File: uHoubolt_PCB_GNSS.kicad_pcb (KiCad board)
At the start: 4 copper layers, 85 x 85 mm, 92 parts, among them J1 Power In, J10 CAN1, J11 CAN2, J12 MMCX-J-P-H-ST-SM1, J2 Debug, J3 Debug, J4 CAN1, J5 CAN2, J6 CAN1, J7 CAN2, J8 CAN1, J9 CAN2, Q1 SISA88DN or similar, U1 SAM-M8Q, U10 LoRa1278F30, U11 LPS25HB, U2 STM32G491MET6-LQFP80, U3 W25Q256JV, U4 MCP1700-3302E, U5 MCP2562FDT-H_SN, U6 MCP2562FDT-H_SN, U7 TS30041, U8 MCP1700-3302E, U9 ICM-20602, X1 TXC-7C

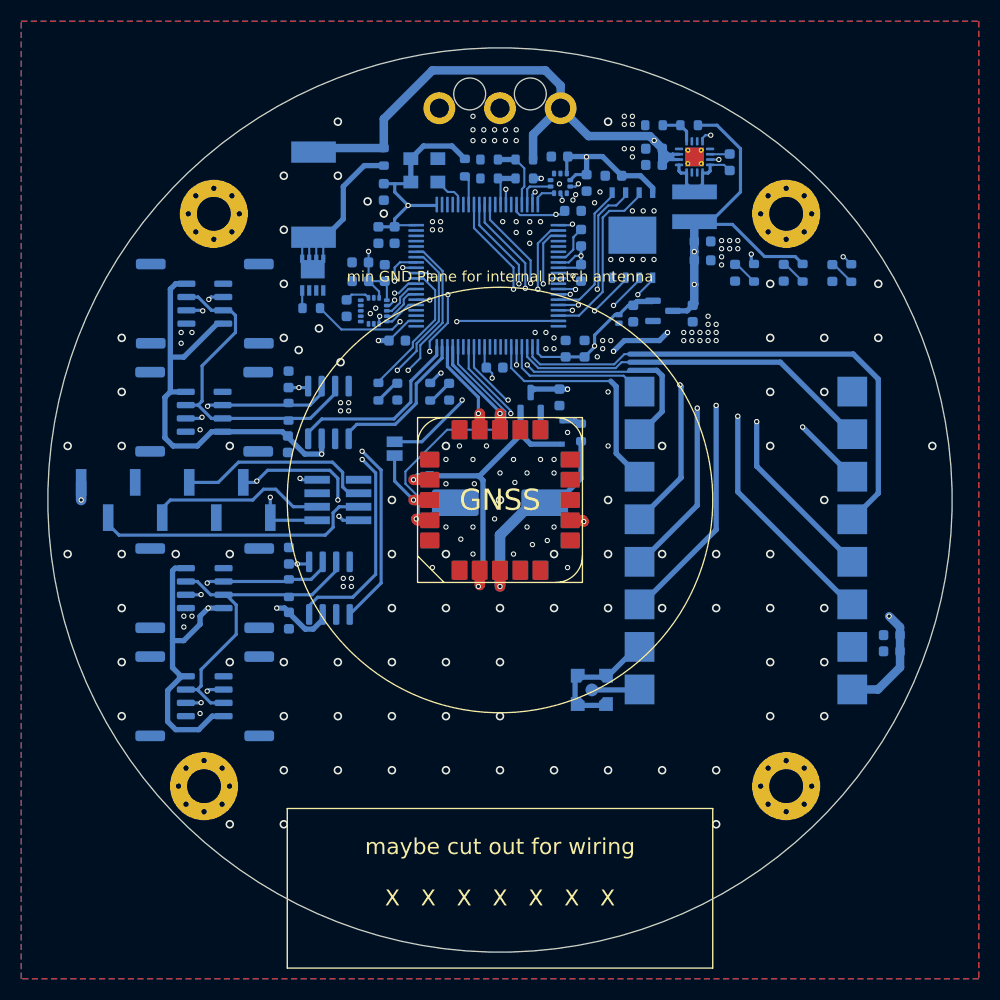
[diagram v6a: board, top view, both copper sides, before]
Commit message: Update CAN transceiver footprints; removed redundant CAN jacks; replaced Power In Conn
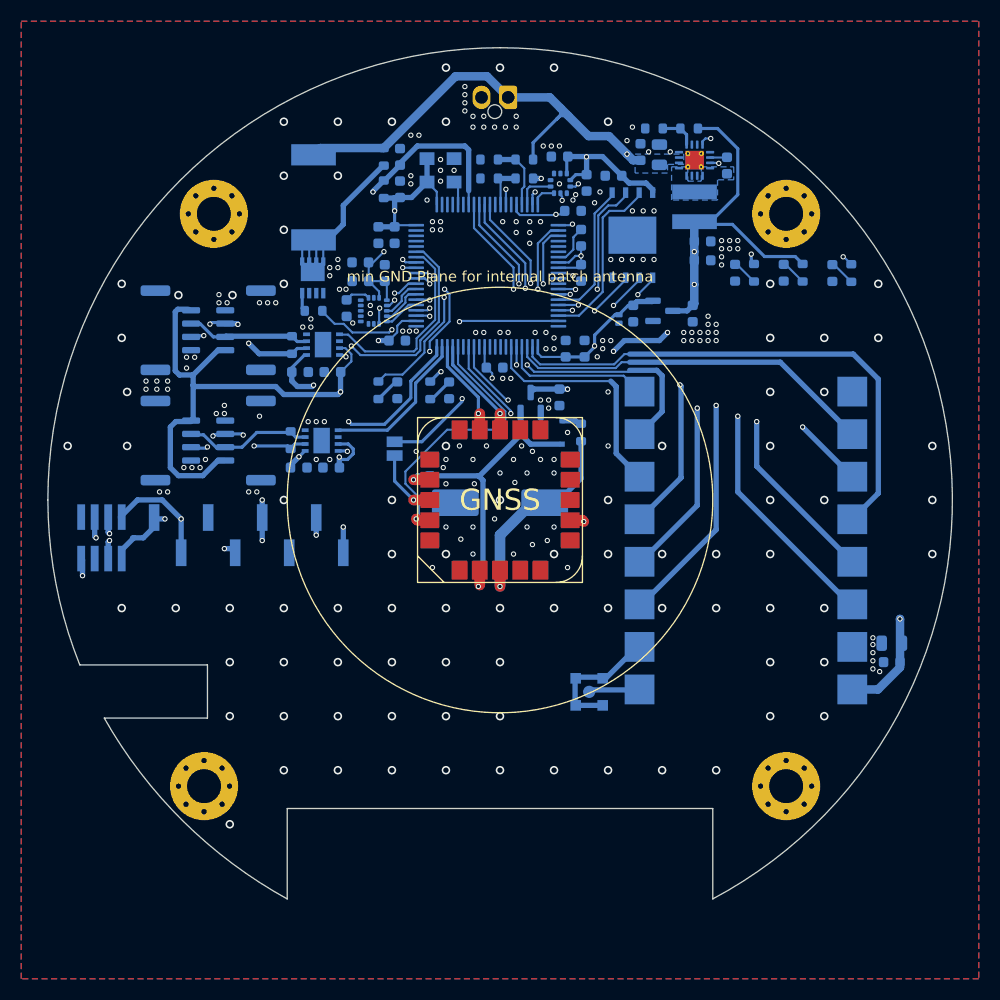
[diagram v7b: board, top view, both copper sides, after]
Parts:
- removed J10, J8: CAN1, Connector_JST:JST_GH_BM04B-GHS-TBT_1x04-1MP_P1.25mm_Vertical
- removed J11, J9: CAN2, Connector_JST:JST_GH_BM04B-GHS-TBT_1x04-1MP_P1.25mm_Vertical
- added C35: 100n, Capacitor_SMD:C_0603_1608Metric, B.Cu at (140.6, 67.7)
- C18, C29: footprint Capacitor_SMD:C_0603_1608Metric -> Capacitor_SMD:C_0805_2012Metric
- J1: footprint TXV_Library_Footprints:Molex_MegaFit_1x03_Vertical -> TXV_Library_Footprints:Molex_Nano-Fit_105309-xx02_1x02_P2.50mm_Vertical
- J12: value MMCX-J-P-H-ST-SM1 -> MMCX-J-P-H-RA-SM1; footprint TXV_Library_Footprints:SAMTEC_MMCX-J-P-H-ST-SM1 -> TXV_Library_Footprints:SAMTEC_MMCX-J-P-H-RA-SM1
- U5, U6: value MCP2562FDT-H_SN -> MCP2562FDT; footprint Package_SO:SOIC-8_3.9x4.9mm_P1.27mm -> Package_DFN_QFN:DFN-8-1EP_3x3mm_P0.65mm_EP1.55x2.4mm
- moved J5 35.1 mm to (119.0, 84.0), turned to -90 degrees
- moved J7 24.2 mm to (126.1, 84.0)
- moved C17 23.7 mm to (134.3, 88.0), turned to 180 degrees
- moved U6 22.9 mm to (133.4, 85.4), turned to 180 degrees
- moved R11 22.9 mm to (130.4, 85.4), turned to -90 degrees
- moved J3 22.5 mm to (112.5, 103.6), turned to -90 degrees
- moved C14 17.3 mm to (131.2, 88.0), turned to 180 degrees
- moved J4 12.9 mm to (126.1, 94.4)
- moved C13 8.35 mm to (131.1, 97.0), turned to 180 degrees
- moved R1 7.89 mm to (139.1, 70.8), turned to 90 degrees
- moved J2 7.61 mm to (126.4, 103.3), turned to 90 degrees
- moved G*** 5.85 mm to (136.5, 115.0)
- moved C16 4.62 mm to (134.1, 97.0), turned to 180 degrees
- moved J6 2.75 mm to (119.0, 94.4)
- moved U5 2.72 mm to (133.2, 94.4), turned to 180 degrees
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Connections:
- R1 pad 2: Net-(R1-Pad2) -> /NRST
- U2 pad 63: unconnected-(U2-Pad63) -> /SWDIO
- U2 pad 64: unconnected-(U2-Pad64) -> /SWCLK
- U2 pad 7: Net-(R1-Pad2) -> /NRST
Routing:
- net /NRST: track 18.7 -> 75.2 mm, vias 0 -> 3
- net +5V: track 258.6 -> 208.0 mm, vias 10 -> 9
- net /SWDIO: track 16.9 -> 48.2 mm, vias 0 -> 4
- net /SWCLK: track 25.9 -> 56.9 mm, vias 0 -> 3
- net /CAN2_RX: track 43.7 -> 20.2 mm
- net /CAN2_TX: track 39.8 -> 18.5 mm, vias 2 -> 0
- net /CAN2_H: track 31.6 -> 11.7 mm
- net /CAN1_H: track 31.6 -> 12.5 mm
- net /CAN1_L: track 28.5 -> 12.7 mm
- net /CAN2_L: track 28.7 -> 13.8 mm
- net Net-(C22-Pad2): track 9.11 -> 0.00 mm
- net +12V: track 82.0 -> 73.6 mm
- net /UART_RX: track 35.1 -> 42.6 mm
- net +3V3: track 236.4 -> 240.2 mm
- net Net-(R1-Pad2): track 2.80 -> 0.00 mm
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- added copper zone on B.Cu, net +12V
- added copper zone on B.Cu, net Net-(C22-Pad2)
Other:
- board size 85 x 85 mm -> 85 x 80 mm
- board text removed: "maybe cut out for wiring X X X X X X X"

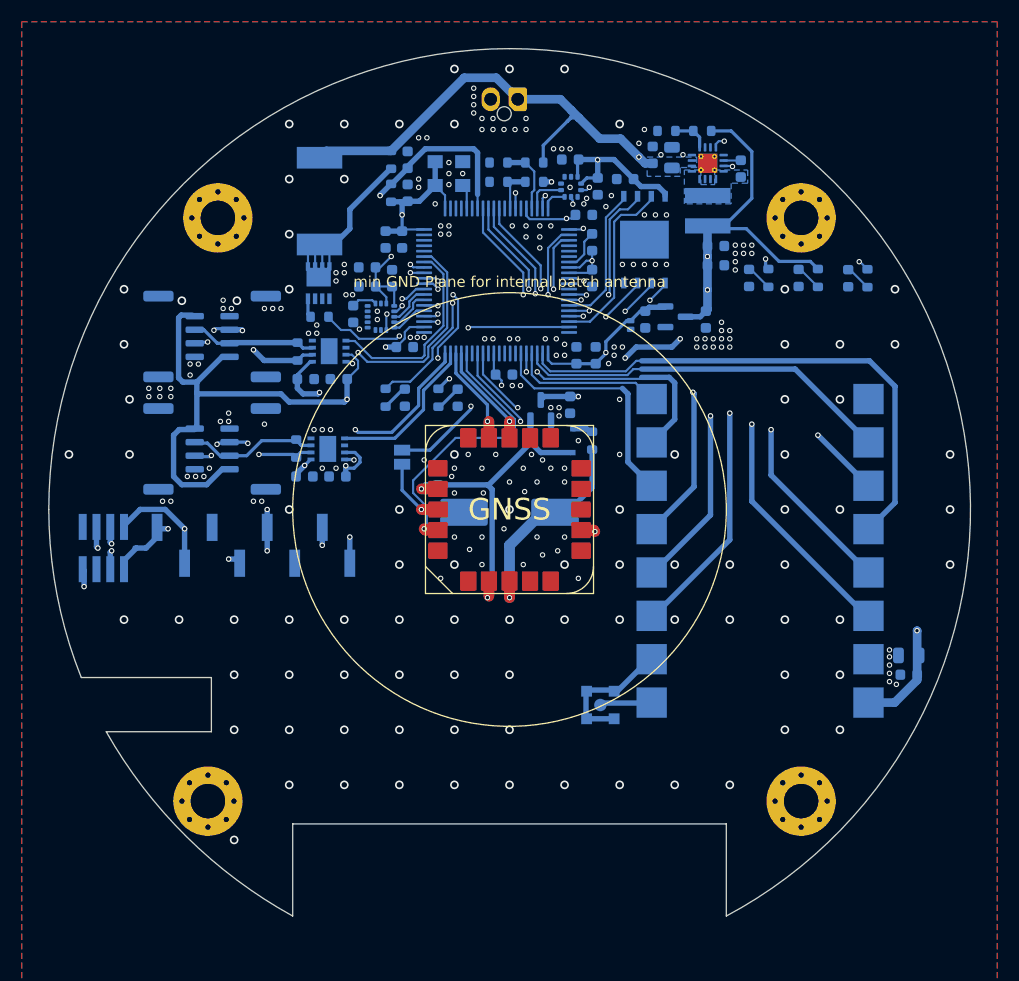
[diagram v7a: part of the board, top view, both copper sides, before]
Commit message: Fixed BARO INT and updated footprints for big caps
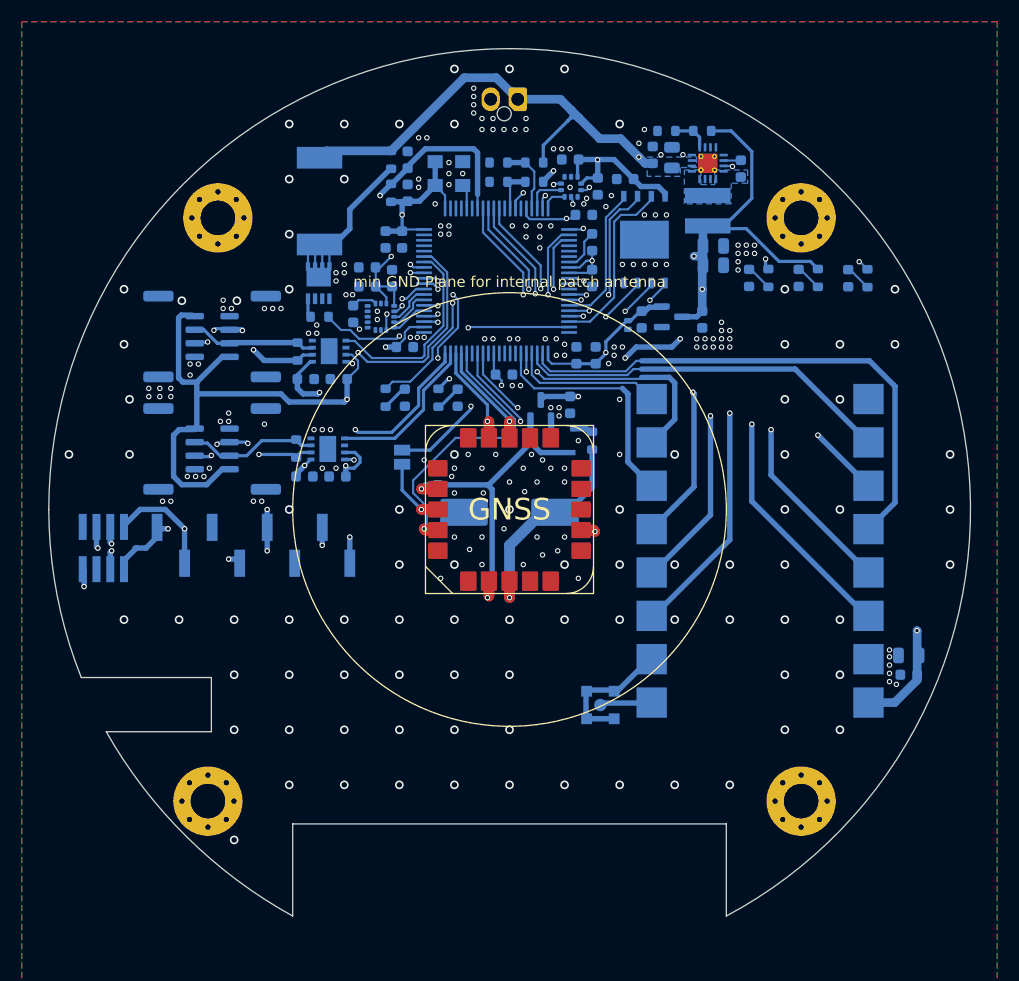
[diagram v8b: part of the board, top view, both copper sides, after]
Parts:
- C23, C24: footprint Capacitor_SMD:C_0603_1608Metric -> Capacitor_SMD:C_0805_2012Metric
- moved C25 0.33 mm to (167.8, 82.5)
- moved U8 0.33 mm to (165.0, 82.2)
- moved C26 0.33 mm to (162.2, 82.5)
- moved D4 0.25 mm to (160.9, 83.0)
- moved C23 0.24 mm to (168.8, 75.7)
- moved C24 0.24 mm to (168.8, 77.5)
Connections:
- net /LoRa_RST renamed /LoRa_NRST
- U2 pad 14: /5V_PGOOD -> /BARO_INT
- U7 pad 8: /5V_PGOOD -> unconnected-(U7-Pad8)
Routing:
- net /5V_PGOOD: track 24.8 -> 0.00 mm, vias 2 -> 0
- net /BARO_INT: track 0.00 -> 5.57 mm, vias 0 -> 2
